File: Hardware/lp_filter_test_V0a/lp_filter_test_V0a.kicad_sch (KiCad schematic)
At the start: 8 parts, among them U1 BD450M5FP-CE2, U2 MAX7480ESA+

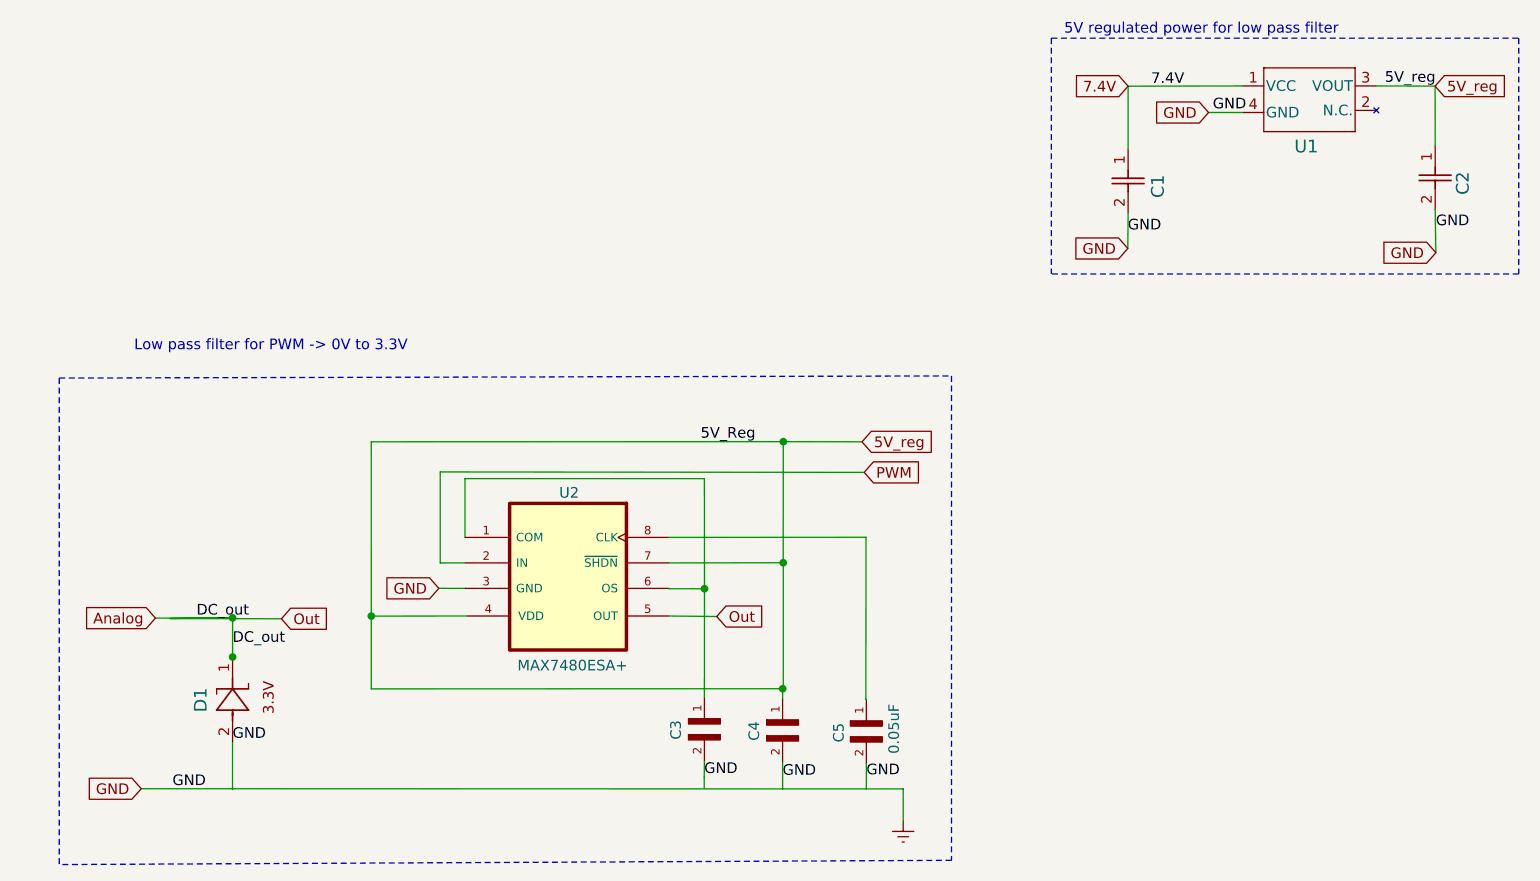
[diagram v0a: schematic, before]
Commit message: Updating KiCad library
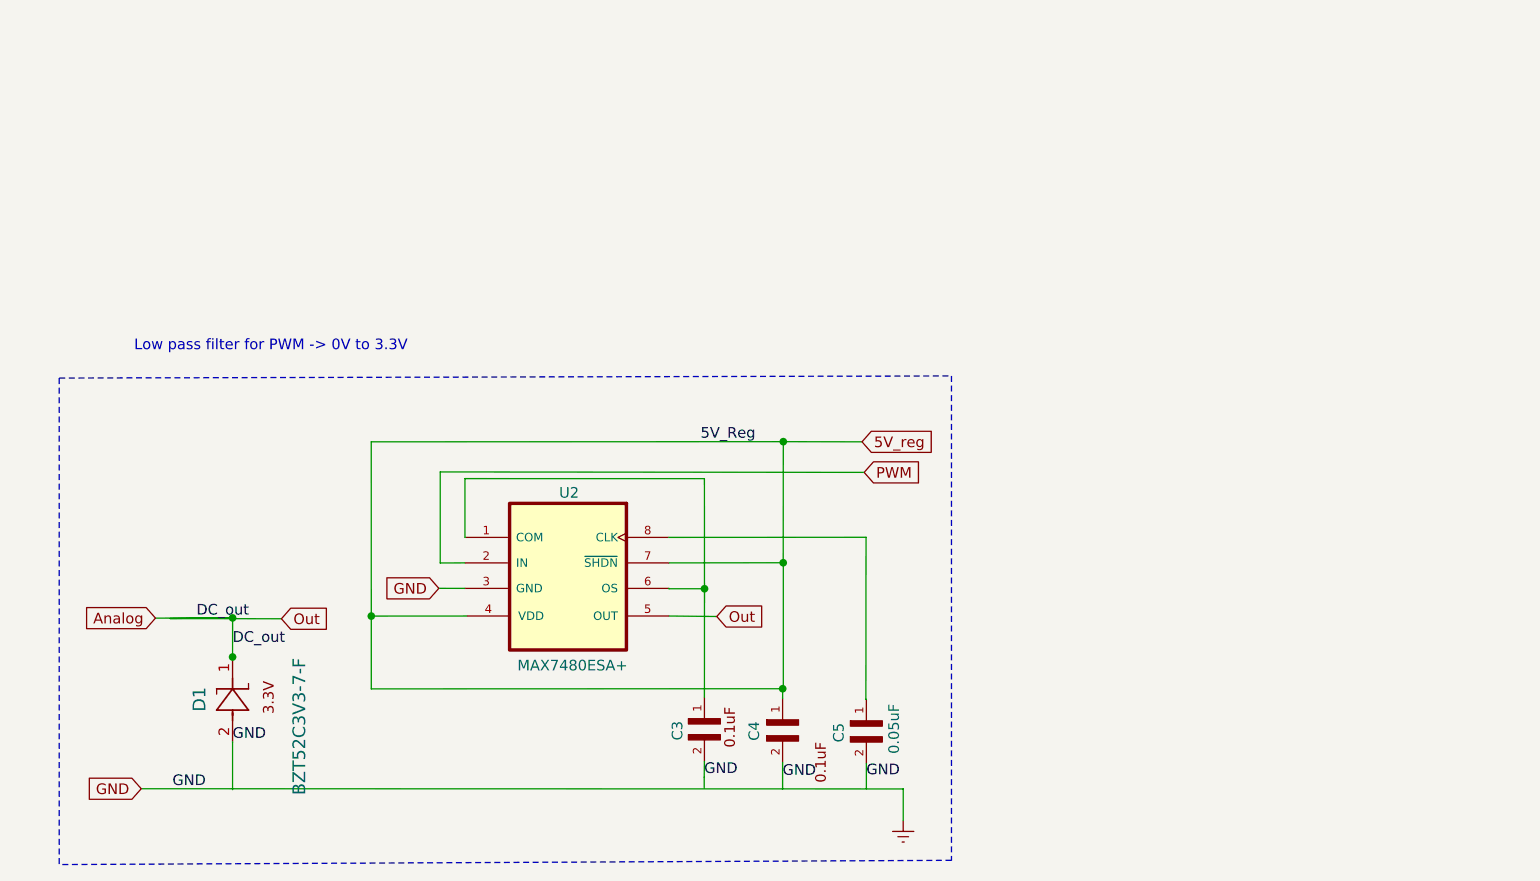
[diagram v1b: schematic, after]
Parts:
- removed C1: CL32B475KBUYNNE, RobotFtpLib:CL32B475KBUYNNE, symbol RobotSymLib:CL32B475KBUYNNE
- removed C2: CL32A106KAULNNE, RobotFtpLib:CL32A106KAULNNE, symbol RobotSymLib:CL32A106KAULNNE
- removed U1: BD450M5FP-CE2, RobotFtpLib:BD450M5FP-CE2, symbol RobotSymLib:BD450M5FP-CE2
- C3, C4: footprint RobotFtpLib:12102C104KAT2A -> CAPC3325X127N
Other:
- note removed: "5V regulated power for low pass filter"
